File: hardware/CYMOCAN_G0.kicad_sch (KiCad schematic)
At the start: 37 parts, among them J1 DebugEdge_02x05, J2 105450-0101, J3 Conn_01x02_Socket, J4 Conn_01x02_Pin, J5 Conn_01x02_Pin, J6 Conn_01x02_Pin, J7 Conn_01x02_Socket, J8 Conn_01x02_Pin, SW1 SW_Push, U1 STM32G0B1CBTx, U2 AP2112K-3.3, U3 TJA1051T-3, U4 TJA1051T-3

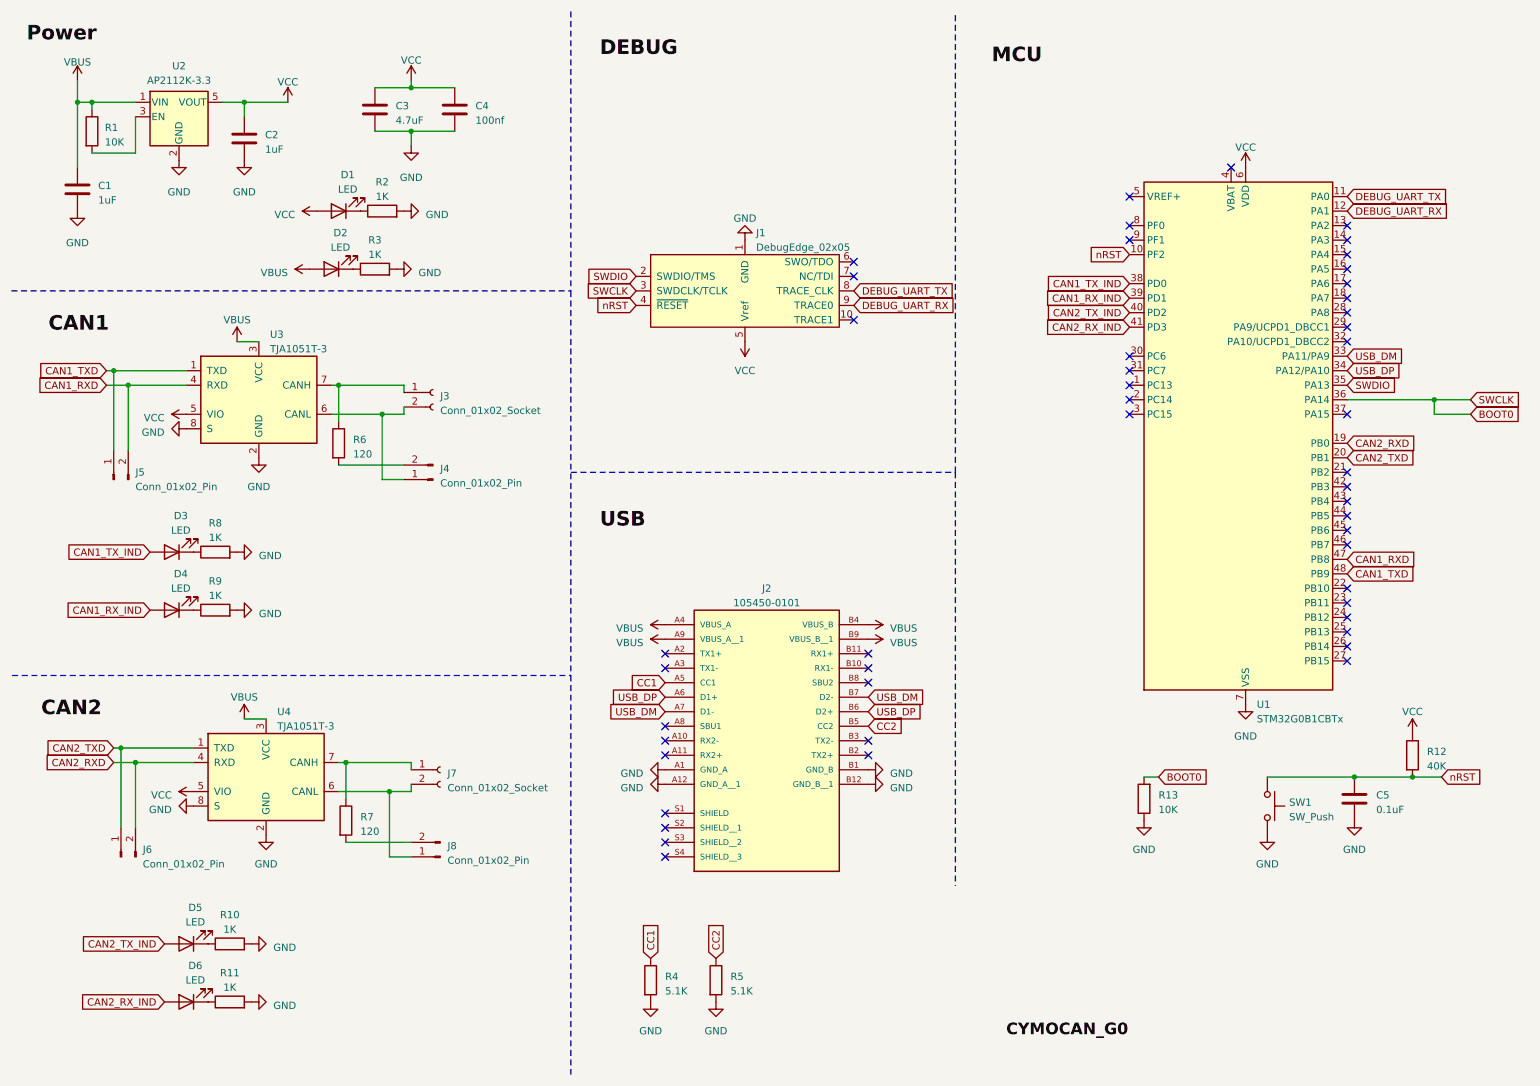
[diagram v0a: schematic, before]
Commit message: Updated terminal block and footprints
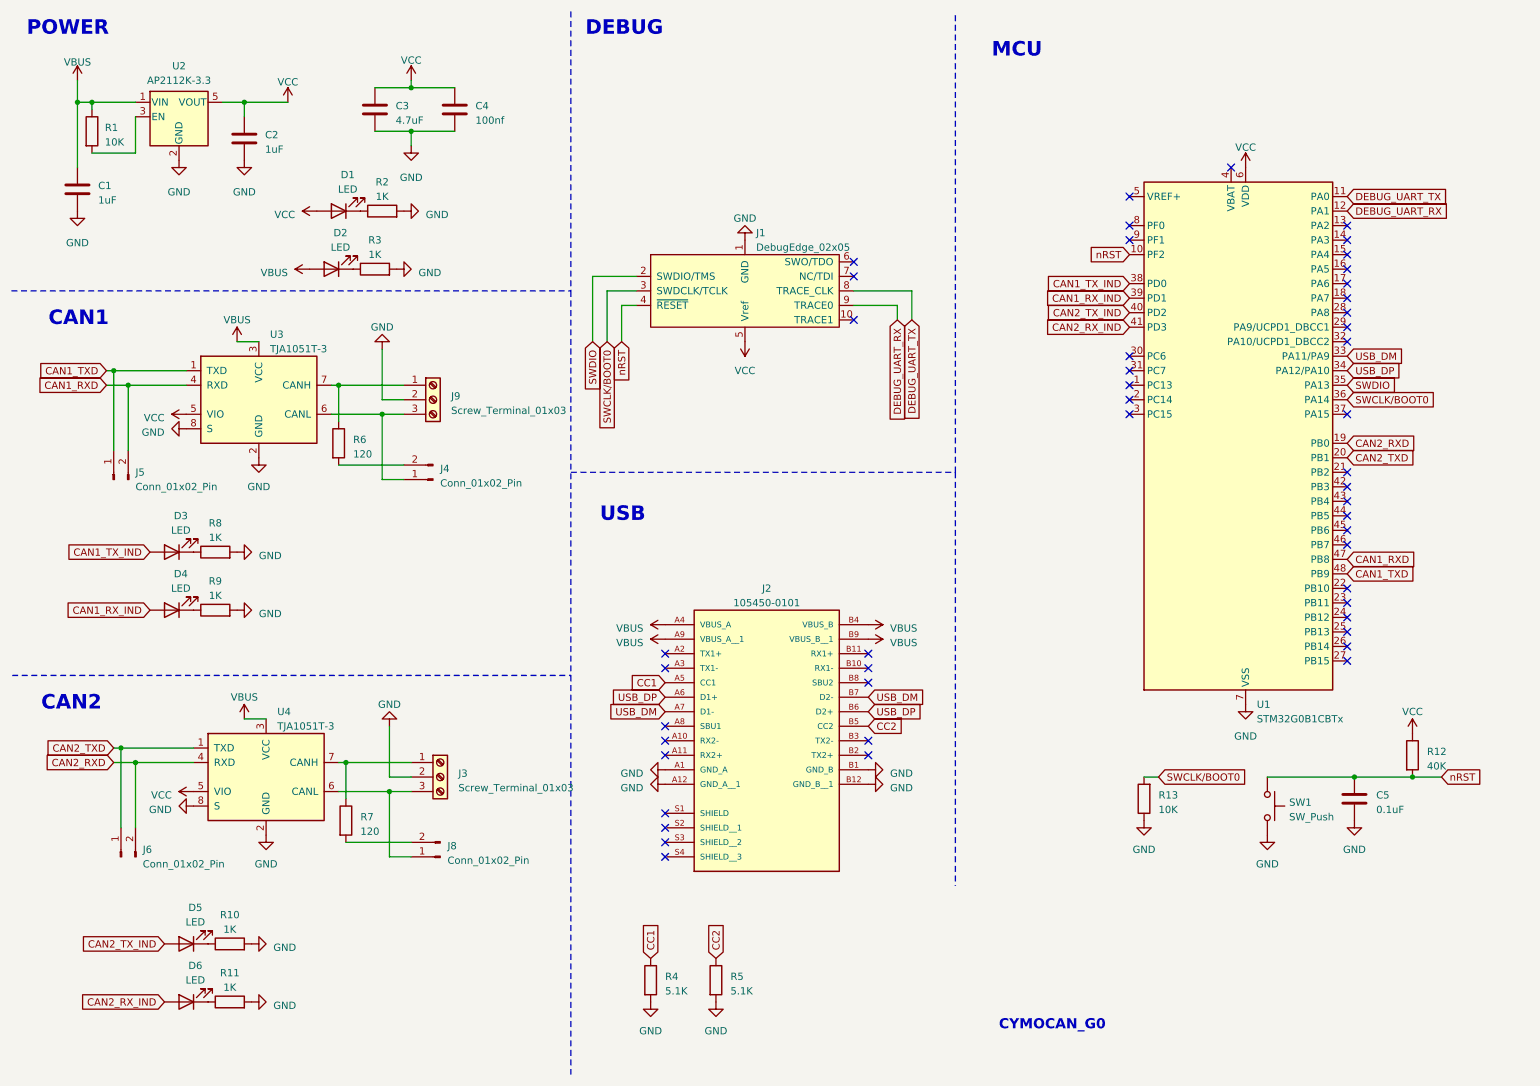
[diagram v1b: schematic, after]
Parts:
- removed J3, J7: Conn_01x02_Socket, symbol Connector:Conn_01x02_Socket
- added J3, J9: Screw_Terminal_01x03, TerminalBlock:TerminalBlock_bornier-3_P5.08mm, symbol Connector:Screw_Terminal_01x03
- C1, C2, C3, C4, C5: footprint (none) -> Capacitor_SMD:C_0603_1608Metric_Pad1.08x0.95mm_HandSolder
- D1, D2, D3, D4, D5, D6: footprint (none) -> LED_SMD:LED_0603_1608Metric_Pad1.05x0.95mm_HandSolder
- J1: footprint (none) -> DebugEdge:DebugEdge_2x05_Target
- J4, J5, J6, J8: footprint (none) -> Connector_PinHeader_2.54mm:PinHeader_2x01_P2.54mm_Vertical
- R1, R10, R11, R12, R13, R2, R3, R4, R5, R6, R7, R8, R9: footprint (none) -> Resistor_SMD:R_0603_1608Metric_Pad0.98x0.95mm_HandSolder
- SW1: footprint (none) -> Button_Switch_THT:SW_PUSH_6mm
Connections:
- net GND: now also J3.2 (Pin_2), J9.2 (Pin_2)
- net at R6.1, U3.7 (CANH): now also J9.1 (Pin_1)
- net at J4.1 (Pin_1), U3.6 (CANL): now also J9.3 (Pin_3)
- net at J8.1 (Pin_1), U4.6 (CANL): now also J3.3 (Pin_3)
- net at R7.1, U4.7 (CANH): now also J3.1 (Pin_1)
- net BOOT0 renamed SWCLK/BOOT0
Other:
- note added: "CAN1"
- note added: "CAN2"
- note added: "CYMOCAN_G0"
- note added: "DEBUG"
- note added: "MCU"
- note added: "POWER"
- note added: "USB"

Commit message: Layout complete
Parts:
- added U4: USBLC6-2P6, Package_TO_SOT_SMD:SOT-666, symbol Power_Protection:USBLC6-2P6
- D1: renamed from D5; value LED -> TX2_IND
- D2: renamed from D6; value LED -> TX2_IND
- D3: renamed from D2; value LED -> VBUS
- D4: renamed from D1; value LED -> VCC
- D5: renamed from D3; value LED -> TX1_IND
- D6: renamed from D4; value LED -> RX1_IND
- J2: renamed from J6; value Conn_01x02_Pin -> CAN2 TX|RX
- J5: renamed from J3; value Screw_Terminal_01x03 -> CAN2
- J7: renamed from J5; value Conn_01x02_Pin -> CAN1 TX|RX
- J8: renamed from J9; value Screw_Terminal_01x03 -> CAN1
- SW1: value SW_Push -> Reset
- renumbered C2 to C1, C1 to C2, C5 to C3, C3 to C5, J2 to J1, J8 to J3, J1 to J6, R5 to R1, R7 to R10, R6 to R11, R3 to R12, R2 to R13, R4 to R2, R1 to R3, R13 to R4, R12 to R5, R10 to R6, R8 to R7, R11 to R8, U2 to U1, U1 to U2, U4 to U3, U3 to U5
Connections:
- net GND: now also U4.2 (GND)
- net USB_DM: now also U4.1 (I/O1); no longer U2.33 (PA11/PA9)
- net USB_DP: now also U4.3 (I/O2); no longer U2.34 (PA12/PA10)
- net VCC: now also U4.5 (VBUS)
- new net USB_DM_ISO: U2.33 (PA11/PA9), U4.6 (I/O1)
- new net USB_DP_ISO: U2.34 (PA12/PA10), U4.4 (I/O2)
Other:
- moved on the sheet: D3, J6, R12
